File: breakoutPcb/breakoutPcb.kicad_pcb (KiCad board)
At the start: 2 copper layers, 49 x 49 mm, 19 parts, among them J1 DB9_Female_MountingHoles, J2 ConY1, J3 ConY2, J4 ConX1, J5 ConX2

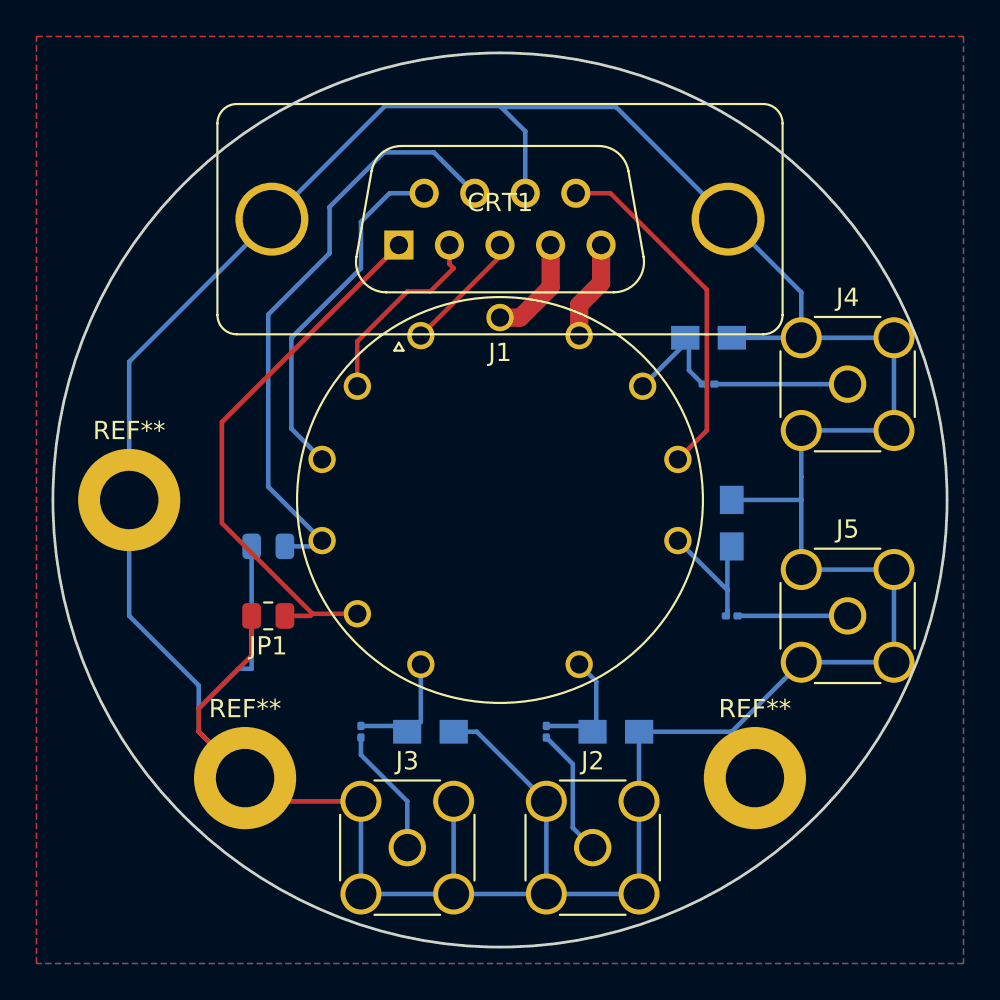
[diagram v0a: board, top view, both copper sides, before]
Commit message: More even distances matching backplane
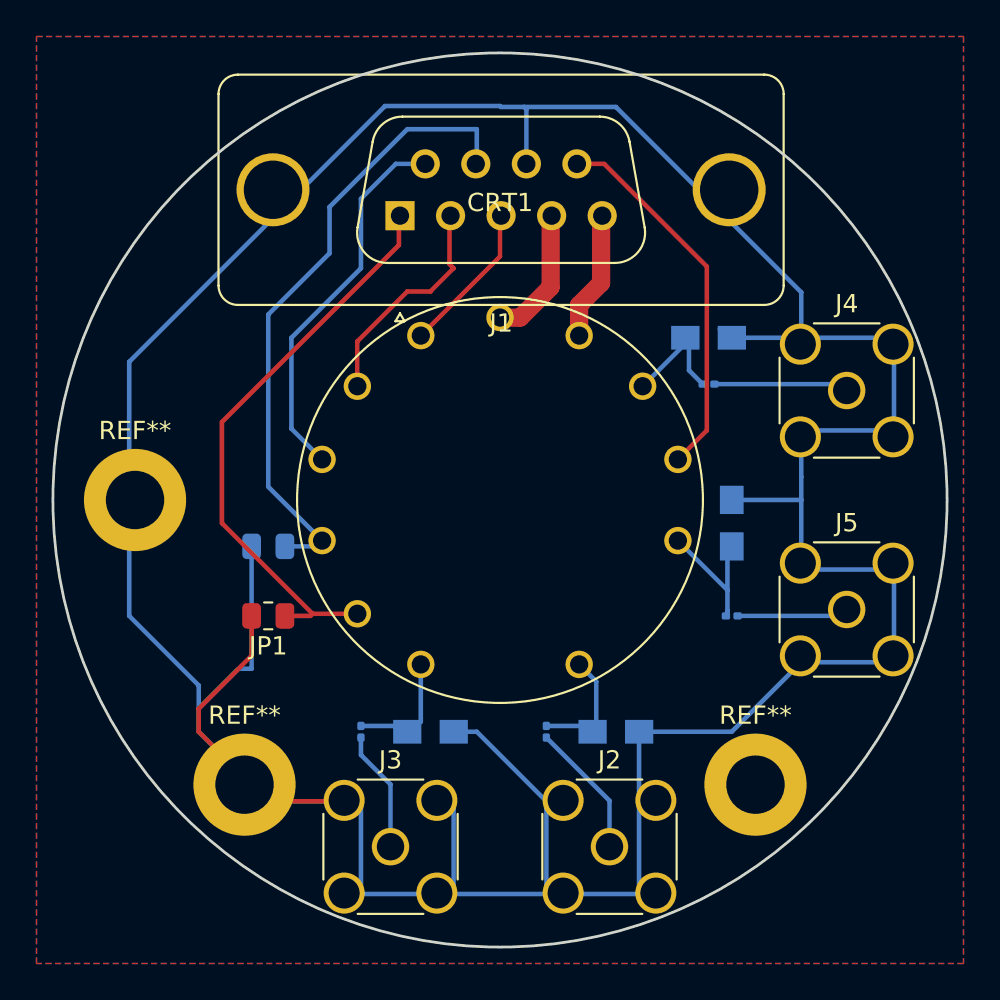
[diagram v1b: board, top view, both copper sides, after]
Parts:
- moved J1 1.61 mm to (70.7, 60.6)
- moved J2 0.92 mm to (82.2, 95.2)
- moved J3 0.92 mm to (70.2, 95.2)
- moved REF** 0.36 mm to (90.2, 91.8)
- moved REF** 0.36 mm to (62.2, 91.8)
- moved J4 0.35 mm to (95.2, 70.2)
- moved J5 0.35 mm to (95.2, 82.2)
- moved REF** 0.32 mm to (56.2, 76.2)
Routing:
- net GND: track 219.4 -> 217.3 mm
- net Net-(CRT1-Pad5): track 33.2 -> 34.8 mm
- net Net-(CRT1-Pad6): track 30.3 -> 31.9 mm
- net Net-(CRT1-Pad14): track 5.46 -> 7.09 mm
- net Net-(CRT1-Pad1): track 5.77 -> 7.40 mm
- net Net-(CRT1-Pad2): track 6.76 -> 8.39 mm
- net Net-(CRT1-Pad3): track 10.8 -> 12.4 mm
- net Net-(CRT1-Pad4): track 19.4 -> 20.9 mm
- net Net-(CRT1-Pad12): track 19.3 -> 20.7 mm

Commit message: Larger holes for tube mount due to different connector
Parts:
- CRT1: footprint ProfessionalDisplaySystems:D14_363GY_123 -> ProfessionalDisplaySystems:D14_363GY_123__LargeHoles
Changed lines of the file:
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@@
     (add_net "Net-(CRT1-Pad6)")
+  )
+  (module ProfessionalDisplaySystems:D14_363GY_123__LargeHoles (layer F.Cu)
+    (at 76.2 76.2)
+    (fp_text reference CRT1 (at 0 -16.295) (layer F.SilkS)
+      (effects (font (size 1 1) (thickness 0.15)))
+    )
+    (fp_text value D14-363GY_123 (at 0 16.295) (layer F.Fab)
+      (effects (font (size 1 1) (thickness 0.15)))
+    )
+    (fp_circle (center 0 0) (end 0 11) (layer F.Fab) (width 0.1))
+    (fp_circle (center 0 0) (end 0 11.12) (layer F.SilkS) (width 0.12))
+    (fp_circle (center 0 0) (end 0 15.62) (layer F.CrtYd) (width 0.05))
+    (pad 14 thru_hole circle (at 4.338837 -9.009688) (size 2 2) (drill 1.5) (layers *.Cu *.Mask)
+      (net 9 "Net-(CRT1-Pad14)"))
+    (pad 13 thru_hole circle (at 7.818314 -6.234898) (size 2 2) (drill 1.5) (layers *.Cu *.Mask)
+      (net 5 "Net-(C3-Pad2)"))
+    (pad 12 thru_hole circle (at 9.749279 -2.225209) (size 2 2) (drill 1.5) (layers *.Cu *.Mask)
+      (net 10 "Net-(CRT1-Pad12)"))
+    (pad 11 thru_hole circle (at 9.749279 2.225209) (size 2 2) (drill 1.5) (layers *.Cu *.Mask)
+      (net 7 "Net-(C4-Pad2)"))
+    (pad 9 thru_hole circle (at 4.338837 9.009688) (size 2 2) (drill 1.5) (layers *.Cu *.Mask)
+      (net 1 "Net-(C1-Pad2)"))
+    (pad 7 thru_hole circle (at -4.338837 9.009688) (size 2 2) (drill 1.5) (layers *.Cu *.Mask)
+      (net 3 "Net-(C2-Pad2)"))
+    (pad 6 thru_hole circle (at -7.818314 6.234898) (size 2 2) (drill 1.5) (layers *.Cu *.Mask)
+      (net 11 "Net-(CRT1-Pad6)"))
+    (pad 5 thru_hole circle (at -9.749279 2.225209) (size 2 2) (drill 1.5) (layers *.Cu *.Mask)
+      (net 17 "Net-(CRT1-Pad5)"))
+    (pad 4 thru_hole circle (at -9.749279 -2.225209) (size 2 2) (drill 1.5) (layers *.Cu *.Mask)
+      (net 12 "Net-(CRT1-Pad4)"))
+    (pad 3 thru_hole circle (at -7.818314 -6.234898) (size 2 2) (drill 1.5) (layers *.Cu *.Mask)
+      (net 13 "Net-(CRT1-Pad3)"))
+    (pad 2 thru_hole circle (at -4.338837 -9.009688) (size 2 2) (drill 1.5) (layers *.Cu *.Mask)
+      (net 14 "Net-(CRT1-Pad2)"))
+    (pad 1 thru_hole circle (at 0 -10) (size 2 2) (drill 1.5) (layers *.Cu *.Mask)
+      (net 15 "Net-(CRT1-Pad1)"))
   )
   (module MountingHole:MountingHole_3.2mm_M3_DIN965_Pad (layer F.Cu)
@@
       (rotate (xyz 0 0 0))
     )
-  )
-  (module ProfessionalDisplaySystems:D14_363GY_123 (layer F.Cu)
-    (at 76.2 76.2)
-    (fp_text reference CRT1 (at 0 -16.295) (layer F.SilkS)
-      (effects (font (size 1 1) (thickness 0.15)))
-    )
-    (fp_text value D14-363GY_123 (at 0 16.295) (layer F.Fab)
-      (effects (font (size 1 1) (thickness 0.15)))
-    )
-    (fp_circle (center 0 0) (end 0 11) (layer F.Fab) (width 0.1))
-    (fp_circle (center 0 0) (end 0 11.12) (layer F.SilkS) (width 0.12))
-    (fp_circle (center 0 0) (end 0 15.62) (layer F.CrtYd) (width 0.05))
-    (pad 14 thru_hole oval (at 4.338837 -9.009688) (size 1.5 1.5) (drill 1) (layers *.Cu *.Mask)
-      (net 9 "Net-(CRT1-Pad14)"))
-    (pad 13 thru_hole oval (at 7.818314 -6.234898) (size 1.5 1.5) (drill 1) (layers *.Cu *.Mask)
-      (net 5 "Net-(C3-Pad2)"))
-    (pad 12 thru_hole oval (at 9.749279 -2.225209) (size 1.5 1.5) (drill 1) (layers *.Cu *.Mask)
-      (net 10 "Net-(CRT1-Pad12)"))
-    (pad 11 thru_hole oval (at 9.749279 2.225209) (size 1.5 1.5) (drill 1) (layers *.Cu *.Mask)
-      (net 7 "Net-(C4-Pad2)"))
-    (pad 9 thru_hole oval (at 4.338837 9.009688) (size 1.5 1.5) (drill 1) (layers *.Cu *.Mask)
-      (net 1 "Net-(C1-Pad2)"))
-    (pad 7 thru_hole oval (at -4.338837 9.009688) (size 1.5 1.5) (drill 1) (layers *.Cu *.Mask)
-      (net 3 "Net-(C2-Pad2)"))
-    (pad 6 thru_hole oval (at -7.818314 6.234898) (size 1.5 1.5) (drill 1) (layers *.Cu *.Mask)
-      (net 11 "Net-(CRT1-Pad6)"))
-    (pad 5 thru_hole oval (at -9.749279 2.225209) (size 1.5 1.5) (drill 1) (layers *.Cu *.Mask)
-      (net 17 "Net-(CRT1-Pad5)"))
-    (pad 4 thru_hole oval (at -9.749279 -2.225209) (size 1.5 1.5) (drill 1) (layers *.Cu *.Mask)
-      (net 12 "Net-(CRT1-Pad4)"))
-    (pad 3 thru_hole oval (at -7.818314 -6.234898) (size 1.5 1.5) (drill 1) (layers *.Cu *.Mask)
-      (net 13 "Net-(CRT1-Pad3)"))
-    (pad 2 thru_hole oval (at -4.338837 -9.009688) (size 1.5 1.5) (drill 1) (layers *.Cu *.Mask)
-      (net 14 "Net-(CRT1-Pad2)"))
-    (pad 1 thru_hole oval (at 0 -10) (size 1.5 1.5) (drill 1) (layers *.Cu *.Mask)
-      (net 15 "Net-(CRT1-Pad1)"))
   )
   (module Capacitor_SMD:C_0201_0603Metric (layer B.Cu)
@@
     (connect_pads (clearance 1.5))
     (min_thickness 0.254)
-    (fill (arc_segments 32) (thermal_gap 0.508) (thermal_bridge_width 0.508))
+    (fill yes (arc_segments 32) (thermal_gap 0.508) (thermal_bridge_width 0.508))
     (polygon
       (pts
@@
     (connect_pads (clearance 1.5))
     (min_thickness 0.254)
-    (fill (arc_segments 32) (thermal_gap 0.508) (thermal_bridge_width 0.508))
+    (fill yes (arc_segments 32) (thermal_gap 0.508) (thermal_bridge_width 0.508))
     (polygon
       (pts

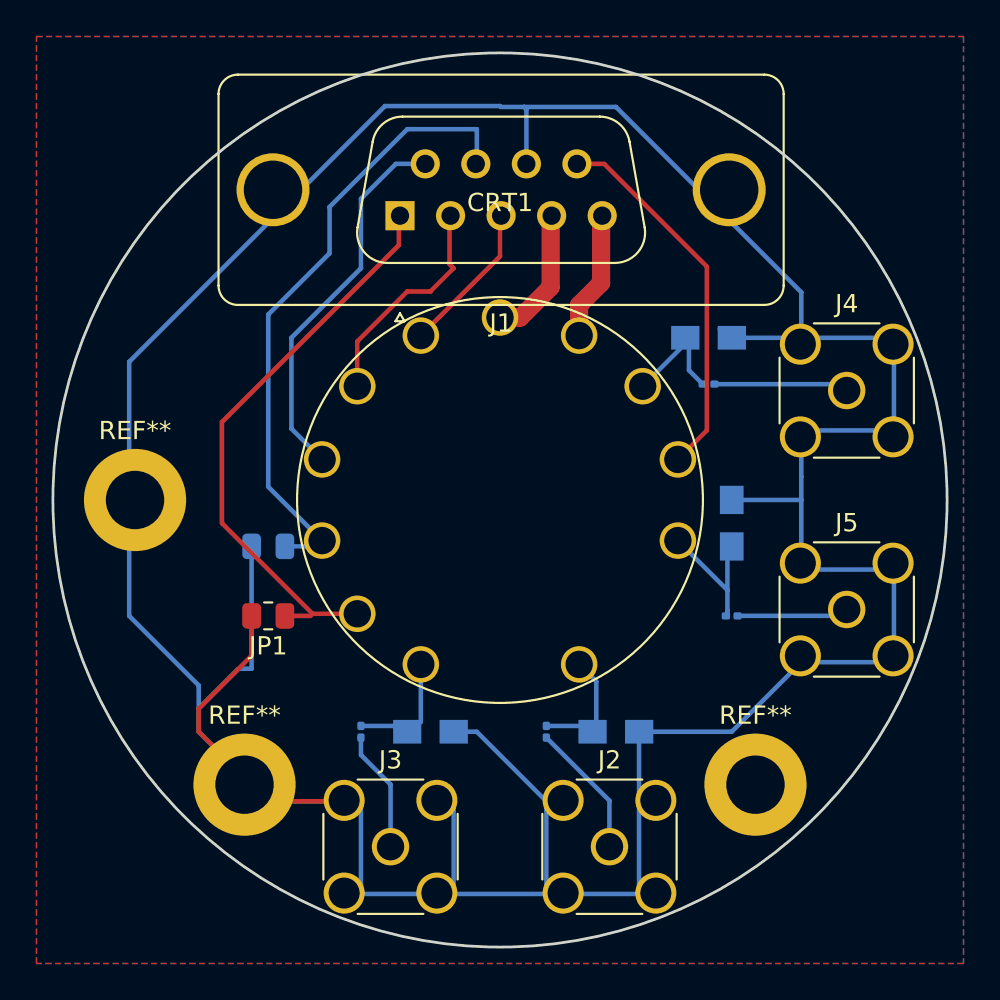
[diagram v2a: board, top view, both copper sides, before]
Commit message: Updated layout (no matching, with new decoupling)
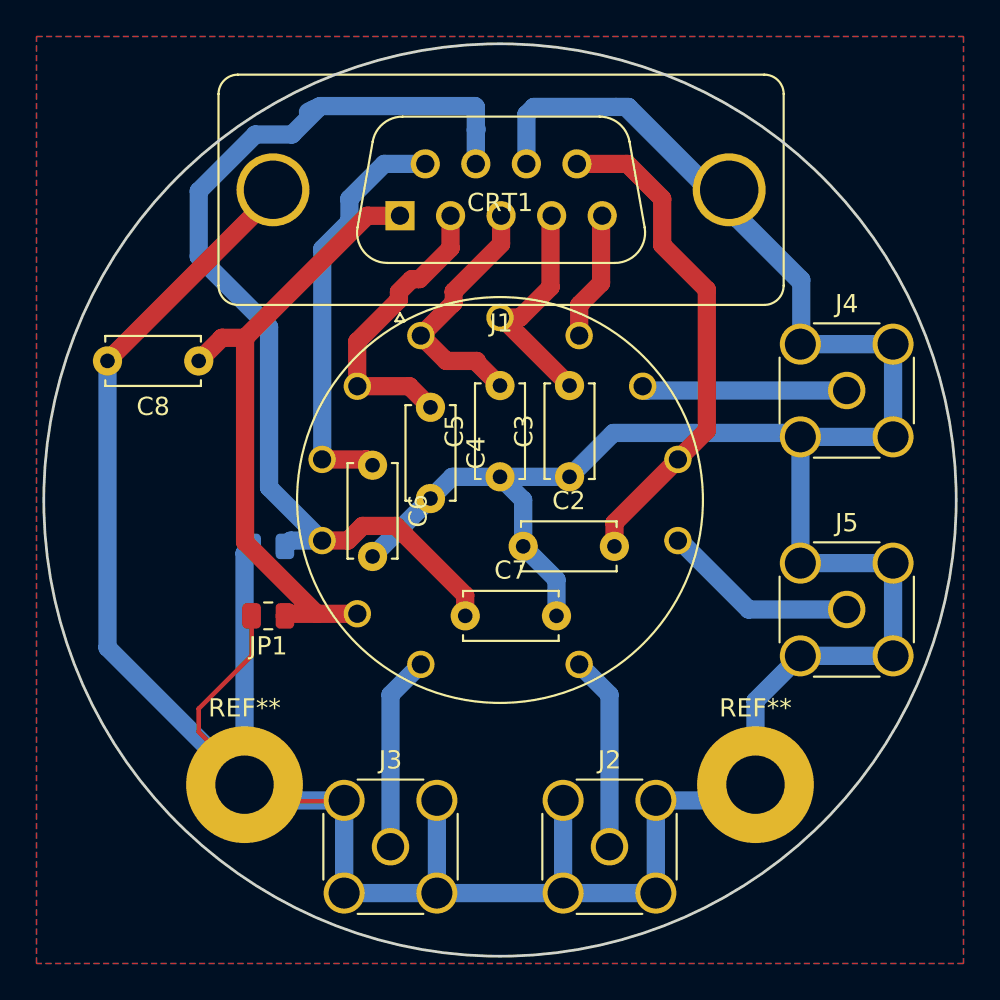
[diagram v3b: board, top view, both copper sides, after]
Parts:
- removed C1: 18 pF, Capacitor_SMD:C_0201_0603Metric
- removed L1, L2, L3, L4: 70 nH, Wurth:Wurth4035
- removed the REF** at (62.2, 91.8)
- removed the REF** at (90.2, 91.8)
- removed the REF** at (56.2, 76.2)
- added C5: 100 pF, Capacitor_THT:C_Disc_D5.0mm_W2.5mm_P5.00mm, F.Cu at (76.2, 74.9)
- added C6: 100 pF, Capacitor_THT:C_Disc_D5.0mm_W2.5mm_P5.00mm, F.Cu at (69.2, 74.3)
- added C7: 100 pF, Capacitor_THT:C_Disc_D5.0mm_W2.5mm_P5.00mm, F.Cu at (74.3, 82.5)
- added C8: 100 pF, Capacitor_THT:C_Disc_D5.0mm_W2.5mm_P5.00mm, F.Cu at (59.7, 68.6)
- added REF**: MountingHole_3.2mm_M3_Pad, MountingHole:MountingHole_3.2mm_M3_Pad, F.Cu at (62.2, 91.8)
- added REF**: MountingHole_3.2mm_M3_Pad, MountingHole:MountingHole_3.2mm_M3_Pad, F.Cu at (90.2, 91.8)
- C2, C3, C4: value 18 pF -> 100 pF; footprint Capacitor_SMD:C_0201_0603Metric -> Capacitor_THT:C_Disc_D5.0mm_W2.5mm_P5.00mm; moved to F.Cu
- CRT1: footprint ProfessionalDisplaySystems:D14_363GY_123__LargeHoles -> ProfessionalDisplaySystems:D14_363GY_123
- moved C4 20.1 mm to (72.4, 71.1), turned to 270 degrees
- moved C2 13.5 mm to (77.5, 78.7), turned to 0 degrees
- moved C3 9.16 mm to (80.0, 74.9), turned to 90 degrees
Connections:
- C2 pad 1: Net-(C2-Pad1) -> GND
- C3 pad 1: Net-(C3-Pad1) -> GND
- C4 pad 2: Net-(C4-Pad2) -> GND
- CRT1 pad 1: Net-(CRT1-Pad1) -> Net-(C3-Pad2)
- CRT1 pad 11: Net-(C4-Pad2) -> Net-(CRT1-Pad11)
- CRT1 pad 12: Net-(CRT1-Pad12) -> Net-(C2-Pad2)
- CRT1 pad 13: Net-(C3-Pad2) -> Net-(CRT1-Pad13)
- CRT1 pad 3: Net-(CRT1-Pad3) -> Net-(C4-Pad1)
- CRT1 pad 7: Net-(C2-Pad2) -> Net-(CRT1-Pad7)
- CRT1 pad 9: Net-(C1-Pad2) (its old number) -> Net-(CRT1-Pad9)
- J1 pad 2: Net-(CRT1-Pad3) -> Net-(C4-Pad1)
- J1 pad 4: Net-(CRT1-Pad1) -> Net-(C3-Pad2)
- J1 pad 9: Net-(CRT1-Pad12) -> Net-(C2-Pad2)
- J2 pad 1: Net-(C1-Pad1) -> Net-(CRT1-Pad9)
- J3 pad 1: Net-(C2-Pad1) -> Net-(CRT1-Pad7)
- J4 pad 1: Net-(C3-Pad1) -> Net-(CRT1-Pad13)
- J5 pad 1: Net-(C4-Pad1) -> Net-(CRT1-Pad11)
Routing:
- net GND: track 217.3 -> 286.3 mm
- net Net-(C7-Pad1): track 34.8 -> 65.6 mm
- net Net-(C2-Pad2): track 6.78 -> 27.6 mm
- net Net-(CRT1-Pad12): track 20.7 -> 0.00 mm
- net Net-(CRT1-Pad3): track 12.4 -> 0.00 mm
- net Net-(CRT1-Pad13): track 0.00 -> 11.8 mm
- net Net-(CRT1-Pad11): track 0.00 -> 10.8 mm
- net Net-(CRT1-Pad9): track 0.00 -> 10.7 mm
- net Net-(CRT1-Pad7): track 0.00 -> 10.7 mm
- net Net-(C4-Pad1): track 6.03 -> 16.3 mm
- net Net-(C4-Pad2): track 7.74 -> 0.00 mm
- net Net-(C1-Pad1): track 7.41 -> 0.00 mm
- net Net-(CRT1-Pad1): track 7.40 -> 0.00 mm
- net Net-(C3-Pad1): track 7.39 -> 0.00 mm
- net Net-(C1-Pad2) (its old number): track 6.95 -> 0.00 mm
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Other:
- board size 49 x 49 mm -> 50 x 50 mm

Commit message: Bugfixes
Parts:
- added REF**: MountingHole_3.2mm_M3_Pad, MountingHole:MountingHole_3.2mm_M3_Pad, F.Cu at (56.2, 76.2)
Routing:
- net GND: track 286.3 -> 287.4 mm
